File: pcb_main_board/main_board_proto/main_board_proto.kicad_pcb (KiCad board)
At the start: 2 copper layers, 35 parts, among them J1 Sortie Moteur 1, J10 L298N 2, J11 L298N 3, J12 IN M2, J13 IN M3, J14 Conn M2, J15 Conn M3, J16 Ardu_M2, J17 Ardu_M3, J18 Entree puissance, J19 output ext 2, J2 L298N 1, J20 button ON/OFF, J3 Conn M1, J4 Ardu_alim, J5 Output ext 1, J6 Ardu_M1, J7 IN M1, J8 Sortie Moteur 2, J9 Sortie Moteur 3, U1 TSR1-2450E, U2 TSR1-2450E, U3 TSR1-2450E

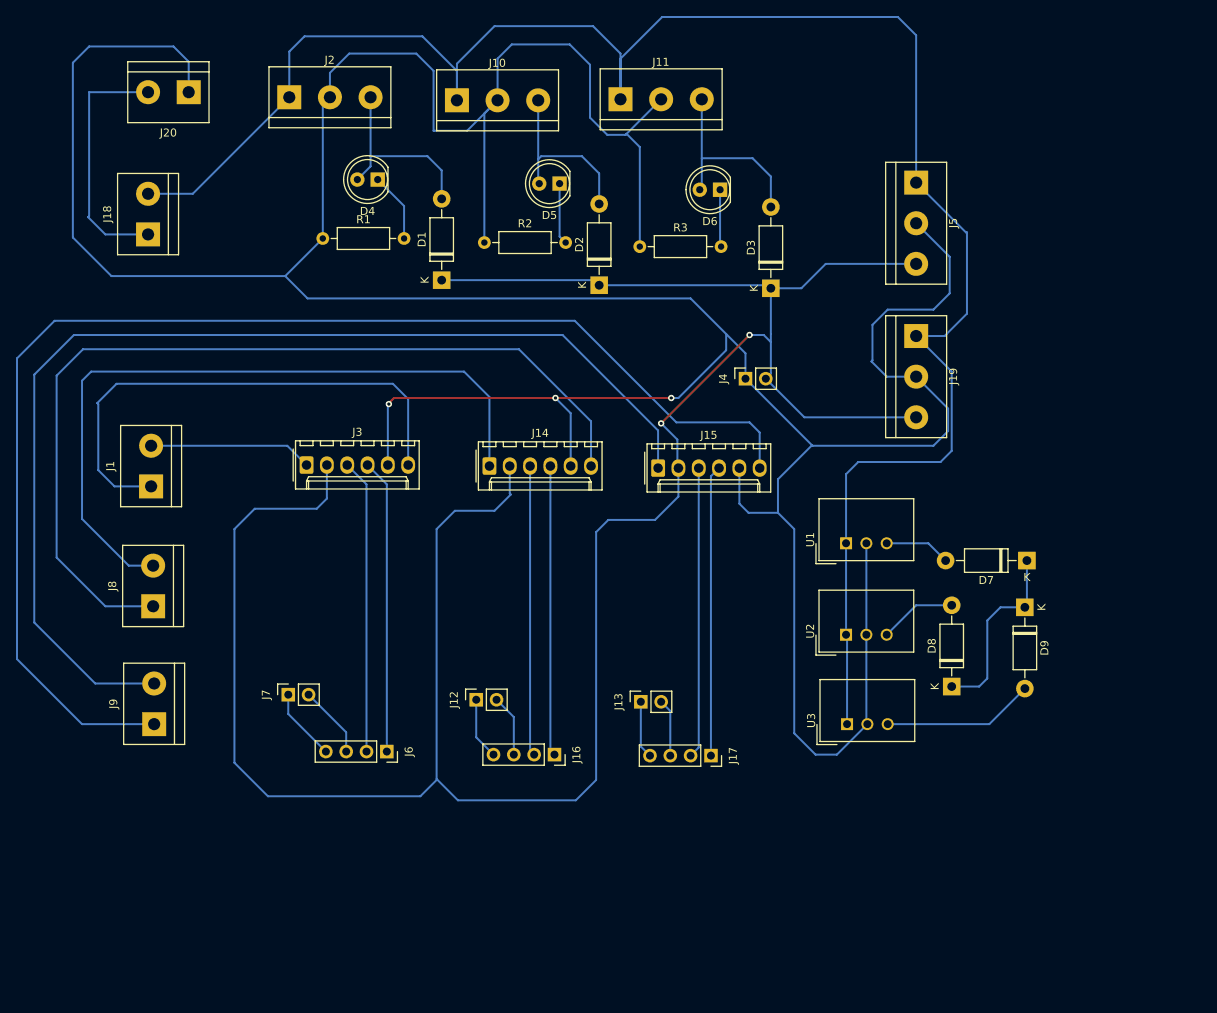
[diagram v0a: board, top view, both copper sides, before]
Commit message: Update main PCB board with 3D step file
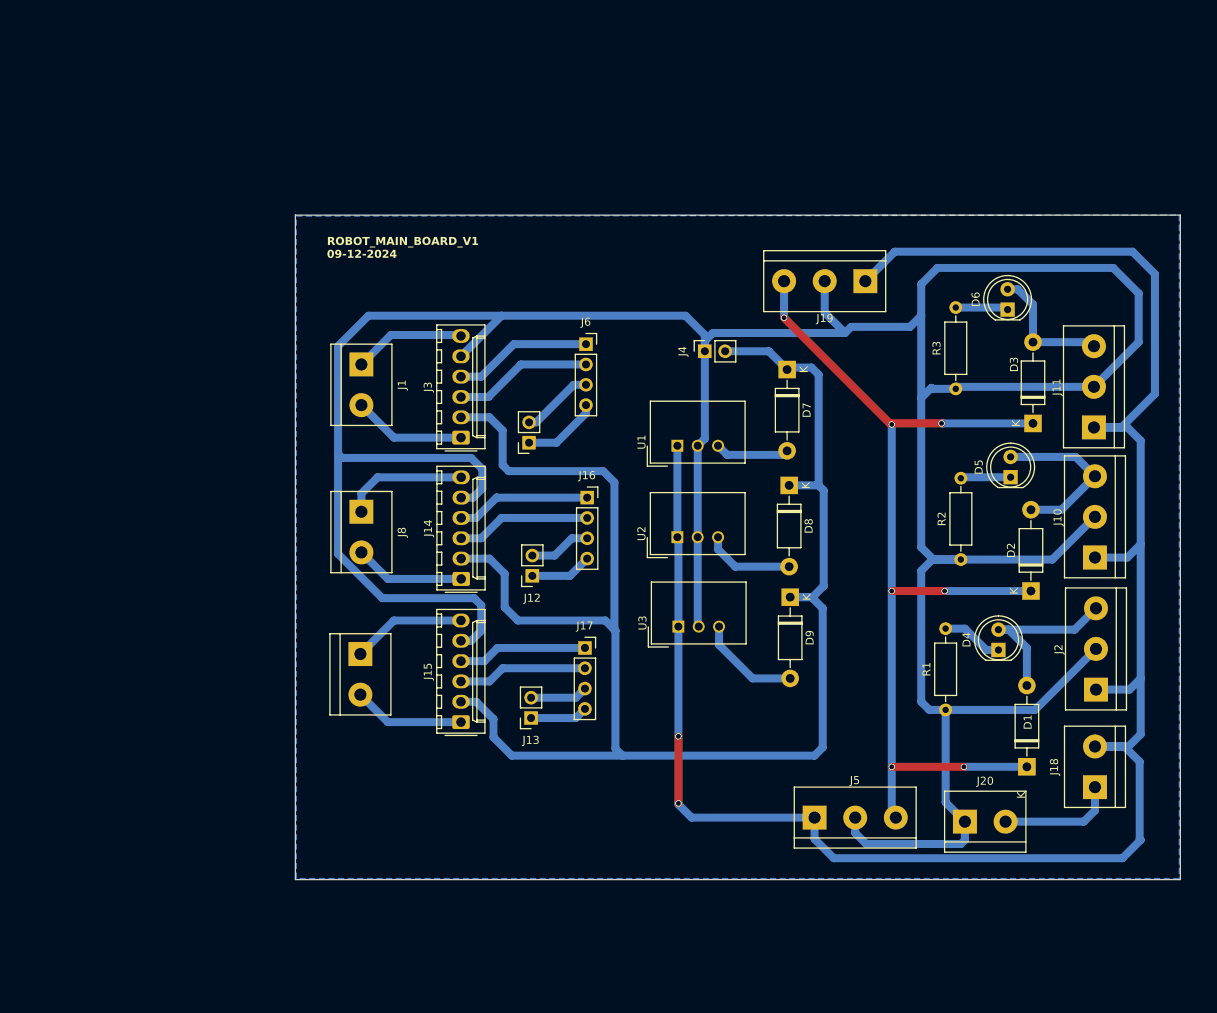
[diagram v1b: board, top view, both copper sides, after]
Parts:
- moved J18 137.1 mm to (147.6, 114.3)
- moved J20 133.2 mm to (131.3, 118.6), turned to 0 degrees
- moved J2 125.1 mm to (147.7, 102.1), turned to 90 degrees
- moved J10 98.1 mm to (147.6, 85.6), turned to 90 degrees
- moved R1 97.6 mm to (128.9, 104.6), turned to 90 degrees
- moved D4 97.4 mm to (135.5, 97.2), turned to 90 degrees
- moved D1 95.1 mm to (139.1, 111.8)
- moved J5 80.4 mm to (112.5, 118.1), turned to 0 degrees
- moved J11 72.0 mm to (147.4, 69.3), turned to 90 degrees
- moved R2 71.5 mm to (130.8, 85.9), turned to 90 degrees
- moved D5 67.3 mm to (137.0, 75.6), turned to 90 degrees
- moved D2 66.1 mm to (139.6, 89.8)
- moved J6 56.7 mm to (83.9, 58.9), turned to 0 degrees
- moved J7 43.6 mm to (76.8, 71.2), turned to 180 degrees
- moved R3 43.3 mm to (130.2, 64.5), turned to 90 degrees
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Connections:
- J14 pad 2: +5V -> +5VA
- J15 pad 2: +5V -> +5VA
- J3 pad 2: +5V -> +5VA
- J4 pad 2: +5V -> +5VA
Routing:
- net +5V: track 307.8 -> 124.8 mm, vias 2 -> 7
- net +5VA: track 23.4 -> 205.2 mm
- net Net-(J15-Pin_6): track 163.1 -> 14.3 mm
- net Net-(J15-Pin_1): track 138.8 -> 14.0 mm
- net Net-(J14-Pin_6): track 114.8 -> 15.6 mm
- net Net-(J14-Pin_1): track 89.9 -> 13.8 mm
- net GND: track 483.7 -> 410.8 mm, vias 3 -> 0
- net Net-(J1-Pin_1): track 64.8 -> 14.0 mm
- net Net-(J15-Pin_4): track 36.4 -> 16.2 mm
- net Net-(J15-Pin_3): track 36.4 -> 16.2 mm
- net Net-(J3-Pin_3): track 36.8 -> 17.3 mm
- net Net-(J3-Pin_4): track 36.8 -> 17.3 mm
- net Net-(J14-Pin_3): track 36.3 -> 16.8 mm
- net Net-(J14-Pin_4): track 36.3 -> 16.8 mm
- net Net-(J18-Pin_1): track 31.4 -> 14.7 mm
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- added copper zone on B.Cu, net GND
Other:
- board outline added: 110.6 x 83.1 mm
- board text added: "ROBOT_MAIN_BOARD_V1 09-12-2024"

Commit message: Update PCB & Add bom with links to digikey
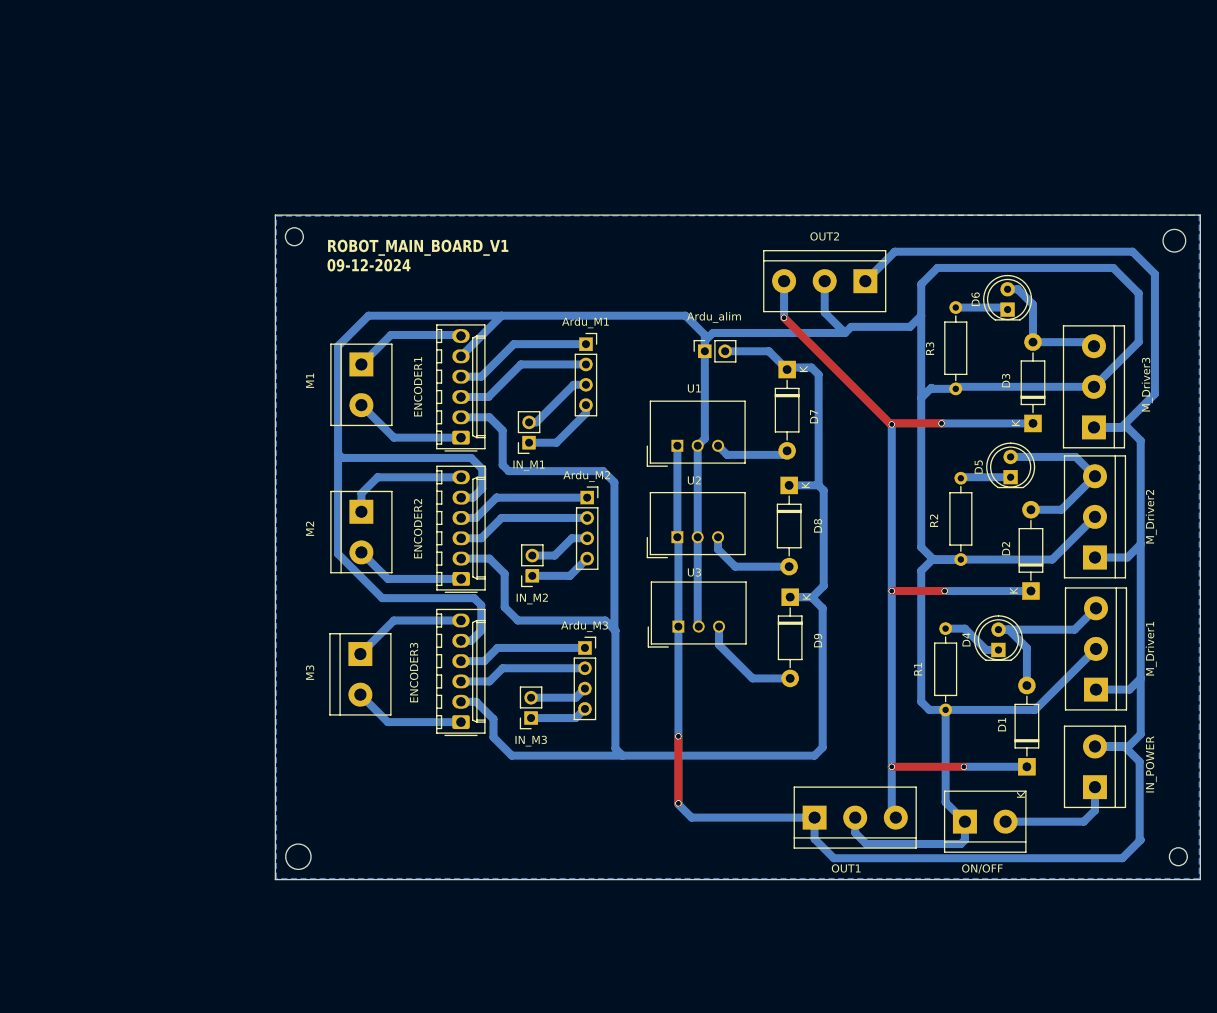
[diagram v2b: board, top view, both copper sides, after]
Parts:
- renumbered J6 to Ardu_M1, J16 to Ardu_M2, J17 to Ardu_M3, J4 to Ardu_alim, J3 to ENCODER1, J14 to ENCODER2, J15 to ENCODER3, J7 to IN_M1, J12 to IN_M2, J13 to IN_M3, J18 to IN_POWER, J1 to M1, J8 to M2, J9 to M3, J2 to M_Driver1, J10 to M_Driver2, J11 to M_Driver3, J20 to ON/OFF, J5 to OUT1, J19 to OUT2
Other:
- board size 110.6 x 83.1 mm -> 115.6 x 83.1 mm

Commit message: Adjust main PCB proto v1 with the 3d model step and part in assembly robot
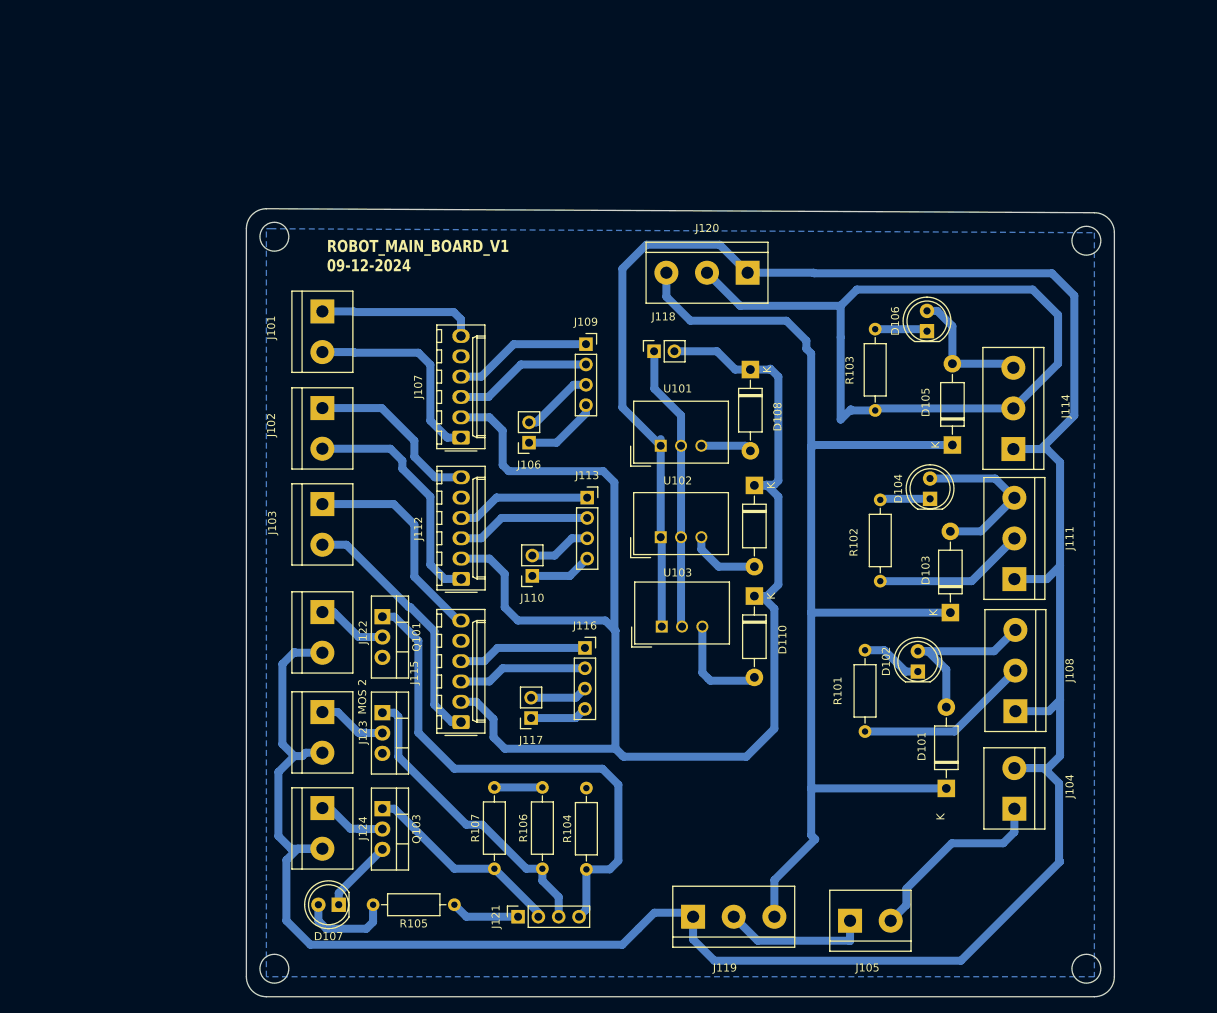
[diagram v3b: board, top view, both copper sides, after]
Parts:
- added D107: LED, LED_THT:LED_D5.0mm, F.Cu at (53.0, 129.0)
- added J121: Ardu_M3, Connector_PinSocket_2.54mm:PinSocket_1x04_P2.54mm_Vertical, F.Cu at (75.5, 130.5)
- added J122: Entree puissance, TerminalBlock:TerminalBlock_bornier-2_P5.08mm, F.Cu at (51.0, 92.4)
- added J123: Entree puissance, TerminalBlock:TerminalBlock_bornier-2_P5.08mm, F.Cu at (51.0, 104.9)
- added J124: Entree puissance, TerminalBlock:TerminalBlock_bornier-2_P5.08mm, F.Cu at (51.0, 116.9)
- added Q101: IRF540N, Package_TO_SOT_THT:TO-220-3_Vertical, F.Cu at (58.5, 93.0)
- added Q102: MOS 2, Package_TO_SOT_THT:TO-220-3_Vertical, F.Cu at (58.5, 105.0)
- added Q103: IRF540N, Package_TO_SOT_THT:TO-220-3_Vertical, F.Cu at (58.5, 117.0)
- added R104: R, Resistor_THT:R_Axial_DIN0207_L6.3mm_D2.5mm_P10.16mm_Horizontal, F.Cu at (84.0, 124.6)
- added R105: R, Resistor_THT:R_Axial_DIN0207_L6.3mm_D2.5mm_P10.16mm_Horizontal, F.Cu at (67.5, 129.0)
- added R106: R, Resistor_THT:R_Axial_DIN0207_L6.3mm_D2.5mm_P10.16mm_Horizontal, F.Cu at (78.5, 124.5)
- added R107: R, Resistor_THT:R_Axial_DIN0207_L6.3mm_D2.5mm_P10.16mm_Horizontal, F.Cu at (72.5, 124.5)
- moved J119 19.6 mm to (97.3, 130.5)
- moved J103 19.3 mm to (51.0, 78.9)
- moved J105 19.0 mm to (117.0, 131.0)
- moved J120 14.7 mm to (104.2, 50.0)
- moved J102 13.9 mm to (51.0, 66.9)
- moved D103 10.4 mm to (129.5, 92.5)
- moved D105 10.4 mm to (129.8, 71.5)
- moved J104 10.4 mm to (137.5, 117.0)
- moved J111 10.4 mm to (137.5, 88.3)
- moved J114 10.4 mm to (137.4, 72.0)
- moved R103 10.4 mm to (120.1, 67.2)
- moved R101 10.4 mm to (118.8, 107.3)
- moved R102 10.4 mm to (120.7, 88.6)
- moved D102 10.4 mm to (125.4, 99.9)
- moved D104 10.4 mm to (127.0, 78.3)
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- renumbered D1 to D101, D4 to D102, D2 to D103, D5 to D104, D3 to D105, D6 to D106, D7 to D108, D8 to D109, D9 to D110, M1 to J101, M2 to J102, M3 to J103, IN_POWER to J104, ON/OFF to J105, IN_M1 to J106, ENCODER1 to J107, M_Driver1 to J108, Ardu_M1 to J109, IN_M2 to J110, M_Driver2 to J111, ENCODER2 to J112, Ardu_M2 to J113, M_Driver3 to J114, ENCODER3 to J115, Ardu_M3 to J116, IN_M3 to J117, Ardu_alim to J118, OUT1 to J119, OUT2 to J120, R1 to R101, R2 to R102, R3 to R103, U1 to U101, U2 to U102, U3 to U103
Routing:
- net GND: track 410.8 -> 208.6 mm
- net +12V: track 249.7 -> 370.7 mm, vias 2 -> 0
- net Net-(J121-Pin_4): track 0.00 -> 65.2 mm
- net Net-(J121-Pin_3): track 0.00 -> 37.9 mm
- net +5V: track 124.8 -> 150.4 mm, vias 7 -> 0
- net Net-(J121-Pin_2): track 0.00 -> 25.4 mm
- net Net-(J103-Pin_2): track 14.0 -> 31.9 mm
- net Net-(J102-Pin_2): track 13.8 -> 29.7 mm
- net Net-(J103-Pin_1): track 14.3 -> 27.2 mm
- net Net-(D107-A): track 0.00 -> 11.8 mm
- net Net-(J101-Pin_2): track 14.1 -> 25.9 mm
- net Net-(J104-Pin_1): track 14.7 -> 24.2 mm
- net Net-(J122-Pin_1): track 0.00 -> 8.79 mm
- net Net-(J124-Pin_1): track 0.00 -> 8.59 mm
- net Net-(J123-Pin_1): track 0.00 -> 8.59 mm
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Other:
- board size 115.6 x 83.1 mm -> 108.5 x 98.5 mm
